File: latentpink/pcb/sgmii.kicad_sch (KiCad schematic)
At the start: 6 parts, among them J3 RJ45, J4 RJ45, U5 DP83867, U6 DP83867, U7 BEL_FUSE_S558-5999-M8-F, U8 BEL_FUSE_S558-5999-M8-F

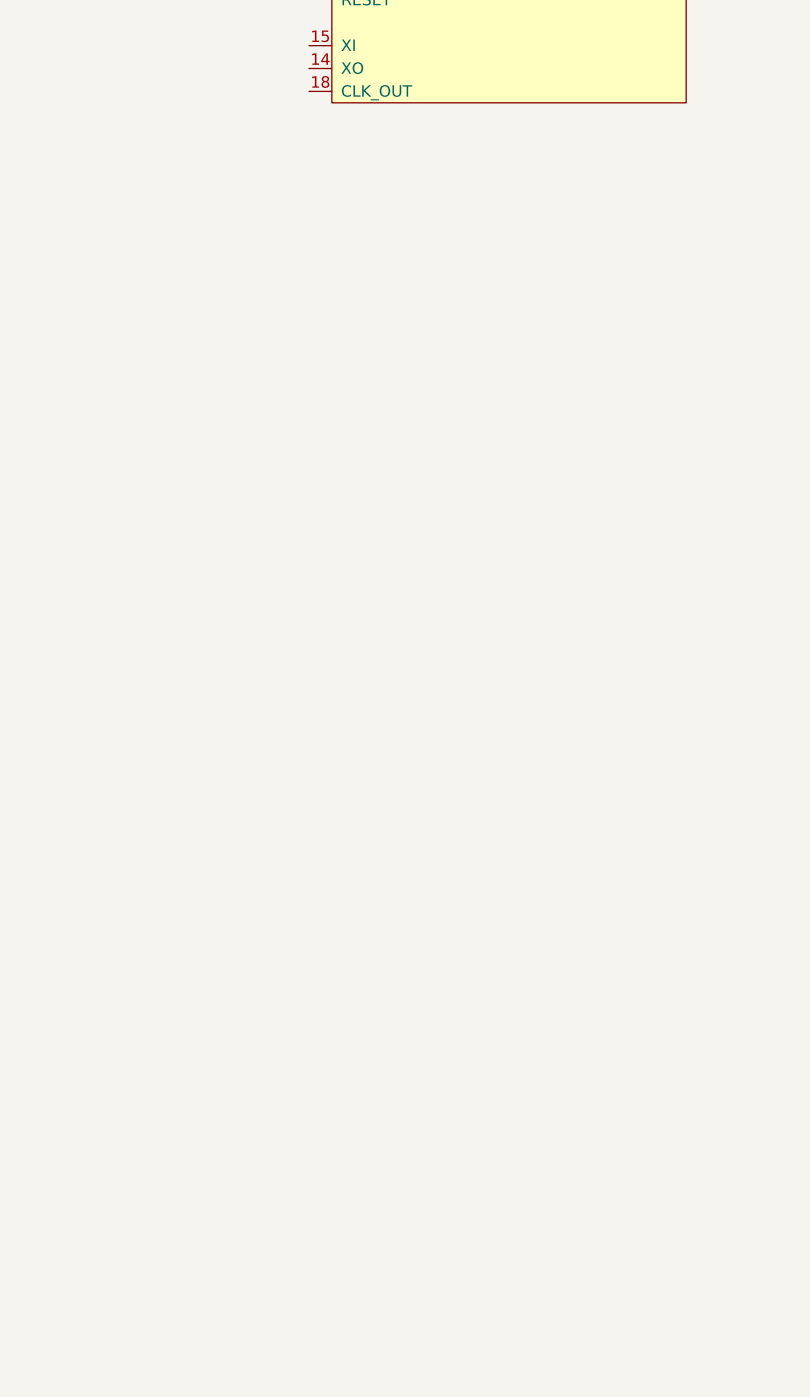
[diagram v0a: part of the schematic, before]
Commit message: Continued initial schematic capture
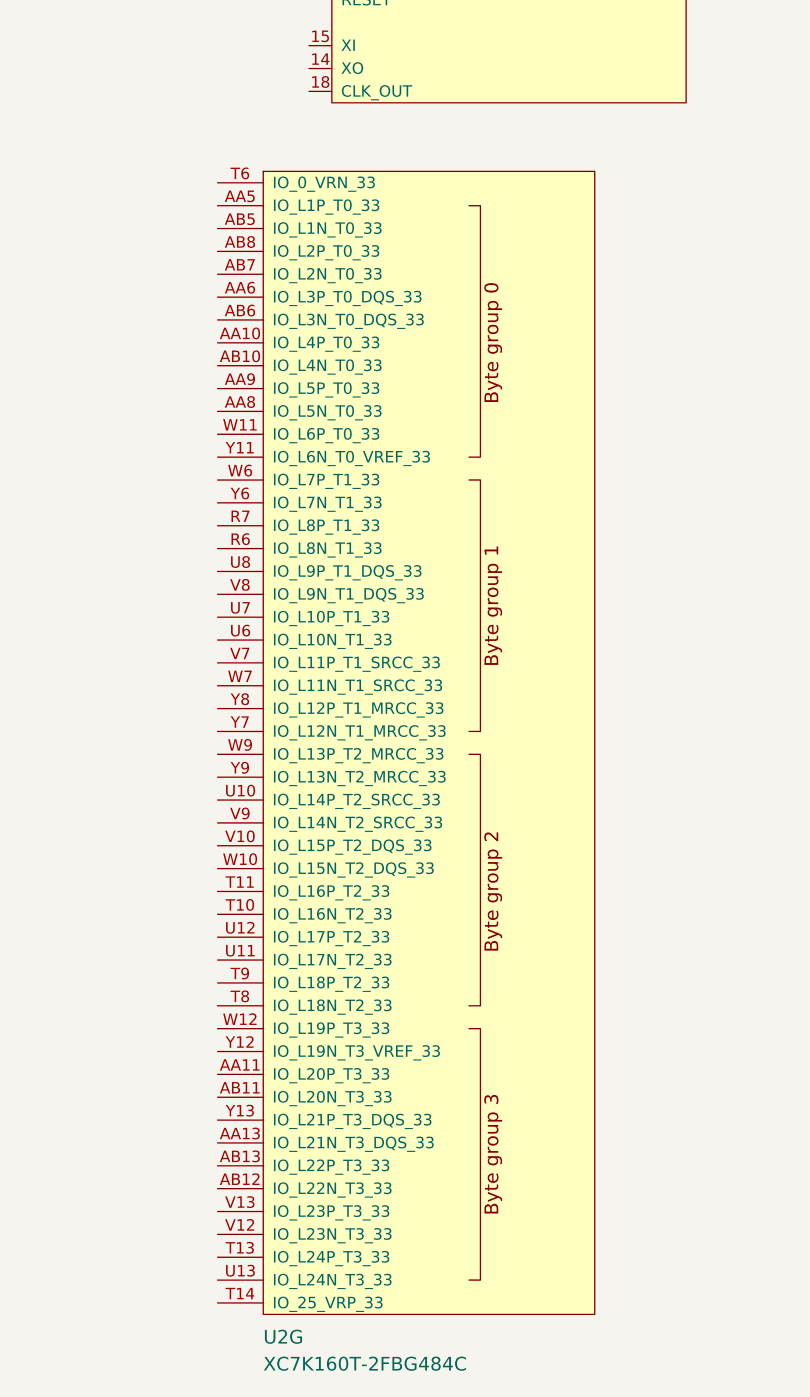
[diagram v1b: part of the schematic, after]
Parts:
- added U2: XC7K160T-2FBG484C, azonenberg_pcb:BGA_484_22x22_FULLARRAY_1MM, symbol xilinx-azonenberg:XC7KxT-FBG484

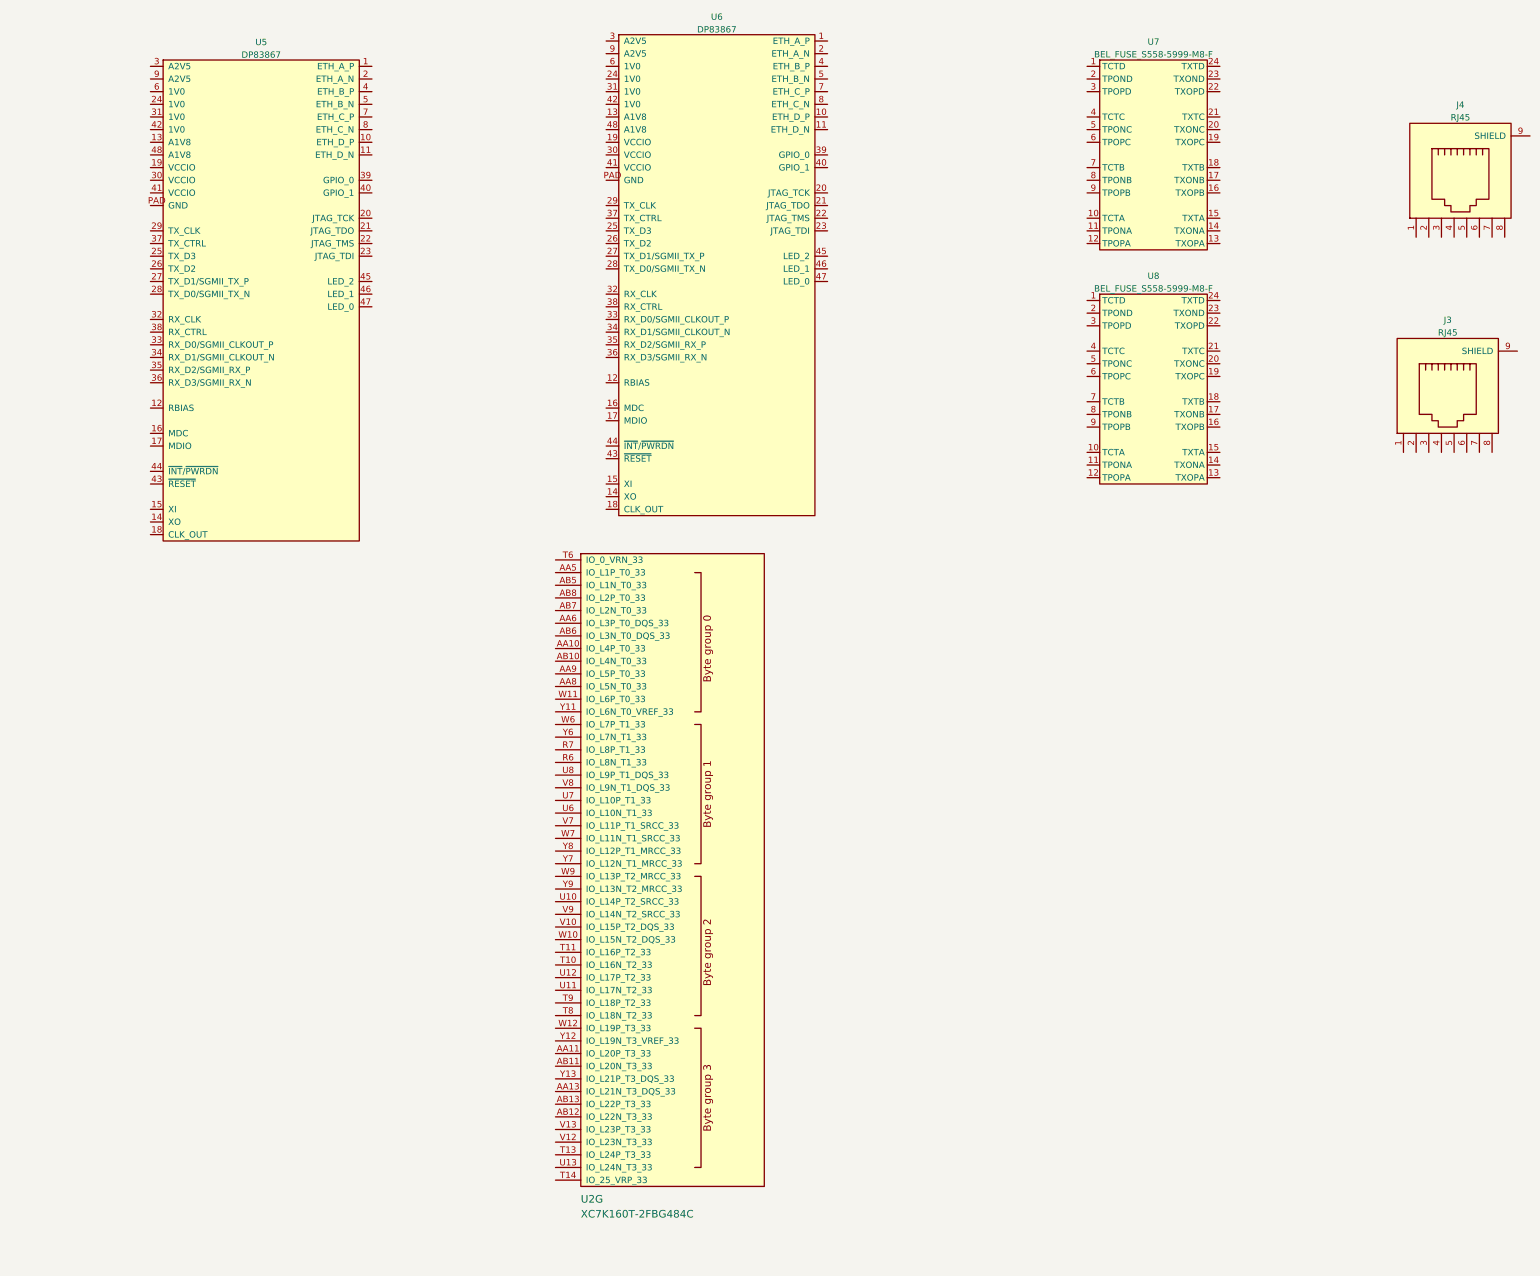
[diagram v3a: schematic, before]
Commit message: Switched to new RJ45 for LATENTPINK, continued general PHY schematic
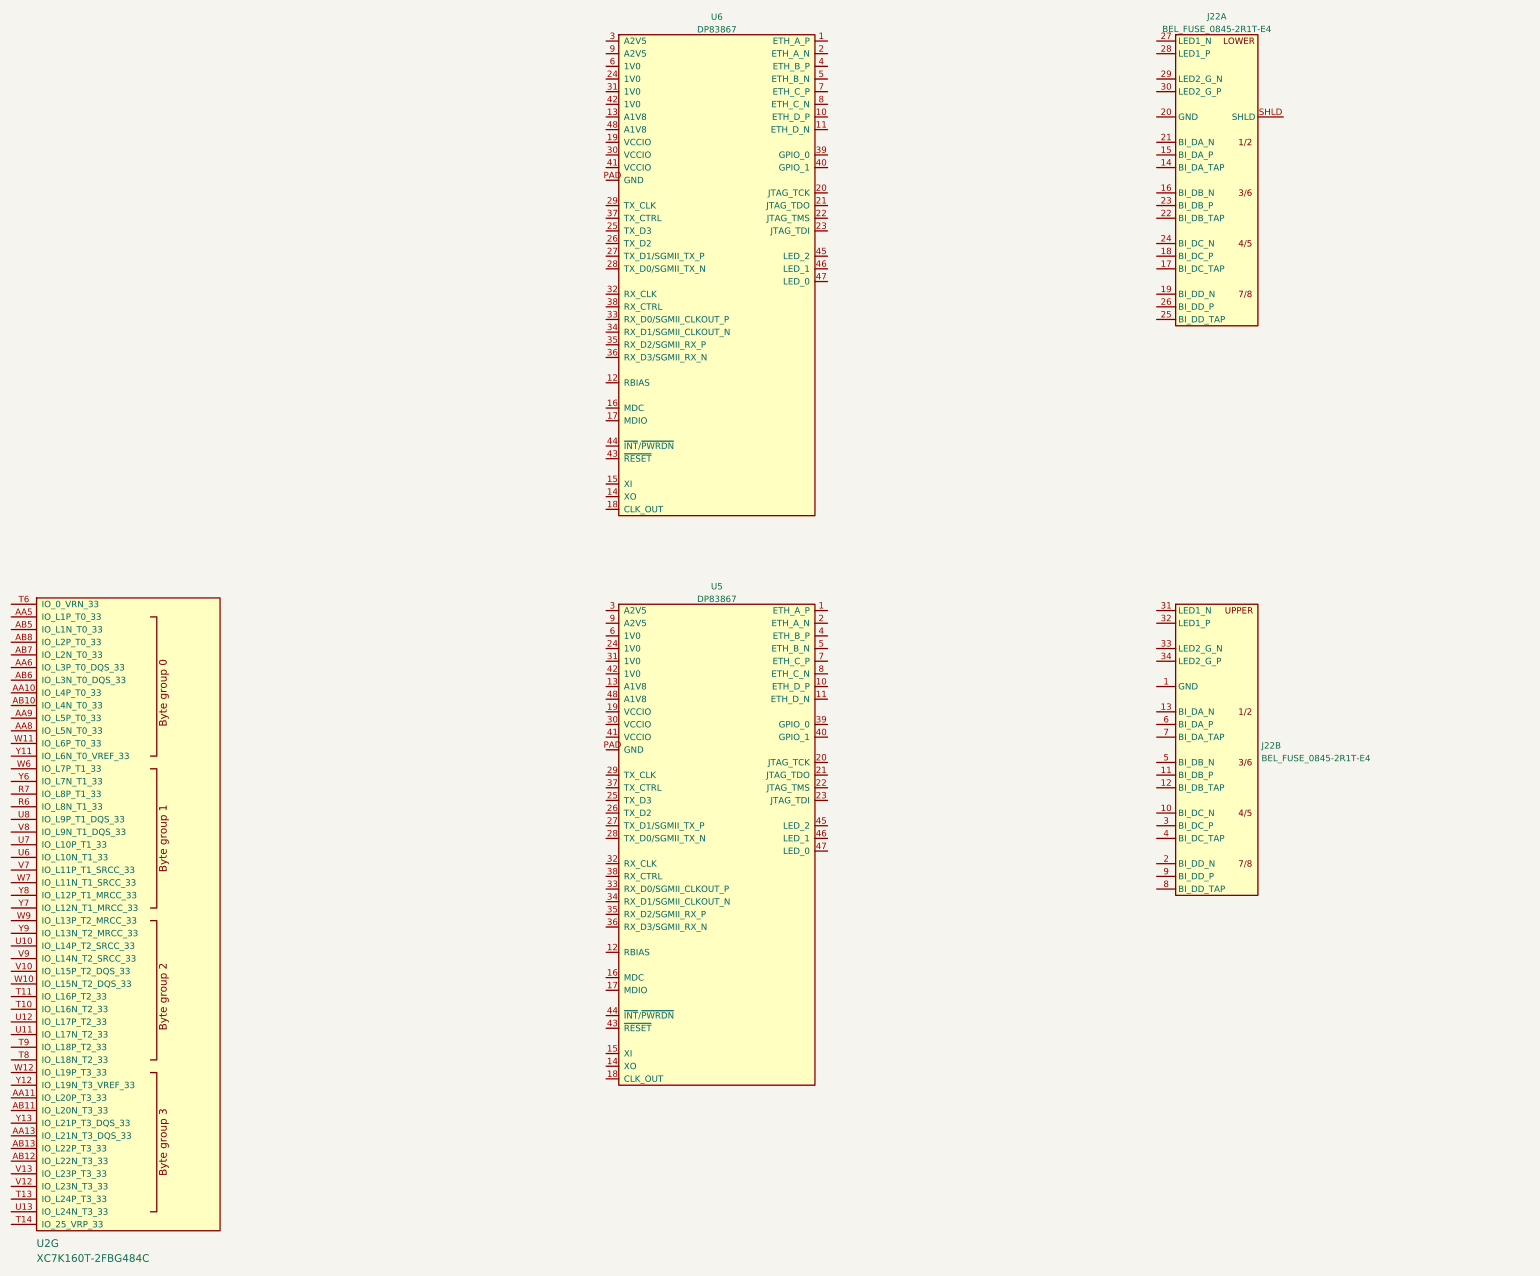
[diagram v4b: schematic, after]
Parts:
- removed J3, J4: RJ45, azonenberg_pcb:CONN_RJ45_BELSTEWART_SS-7188S-A-PG4-1-BA-xx, symbol conn:RJ45
- removed U7, U8: BEL_FUSE_S558-5999-M8-F, azonenberg_pcb:BELFUSE_S558-5999-M8-F, symbol special-azonenberg:BEL_FUSE_S558-5999-M8-F
- added J22: BEL_FUSE_0845-2R1T-E4, azonenberg_pcb:CONN_RJ45_BELFUSE_0845-2R1T-E4, symbol special-azonenberg:BEL_FUSE_0845-2R1T-E4
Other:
- moved on the sheet: U2G, U5
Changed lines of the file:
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@@
   (paper "A3")
   (title_block
-    (date "2023-05-14")
+    (date "2023-05-15")
     (rev "0.1")
     (company "Antikernel Labs")
     (comment 1 "Andrew D. Zonenberg")
   )
-  (symbol (lib_id "conn:RJ45") (at 330.2 54.61 0) (unit 1)
+  (symbol (lib_id "special-azonenberg:BEL_FUSE_0845-2R1T-E4") (at 273.05 198.12 0) (unit 2)
     (in_bom yes) (on_board yes) (fields_autoplaced)
-    (property "Reference" "J4" (id 0) (at 330.2 39.4802 0))
-    (property "Value" "RJ45" (id 1) (at 330.2 42.0171 0))
-    (property "Footprint" "azonenberg_pcb:CONN_RJ45_BELSTEWART_SS-7188S-A-PG4-1-BA-xx" (id 2) (at 330.2 54.61 0)
+    (property "Reference" "J22" (id 0) (at 290.2712 168.0753 0)
+      (effects (font (size 1.27 1.27)) (justify left))
+    )
+    (property "Value" "BEL_FUSE_0845-2R1T-E4" (id 1) (at 290.2712 170.6122 0)
+      (effects (font (size 1.27 1.27)) (justify left))
+    )
+    (property "Footprint" "azonenberg_pcb:CONN_RJ45_BELFUSE_0845-2R1T-E4" (id 2) (at 273.05 198.12 0)
       (effects (font (size 1.27 1.27)) hide)
     )
-    (property "Datasheet" "" (id 3) (at 330.2 54.61 0)
+    (property "Datasheet" "" (id 3) (at 273.05 198.12 0)
       (effects (font (size 1.27 1.27)) hide)
     )
+    (pin "14")
+    (pin "15")
+    (pin "16")
+    (pin "17")
+    (pin "18")
+    (pin "19")
+    (pin "20")
+    (pin "21")
+    (pin "22")
+    (pin "23")
+    (pin "24")
+    (pin "25")
+    (pin "26")
+    (pin "27")
+    (pin "28")
+    (pin "29")
+    (pin "30")
+    (pin "SHLD")
     (pin "1")
+    (pin "10")
+    (pin "11")
+    (pin "12")
+    (pin "13")
     (pin "2")
     (pin "3")
+    (pin "31")
+    (pin "32")
+    (pin "33")
+    (pin "34")
     (pin "4")
     (pin "5")
@@
     (pin "PAD")
   )
-  (symbol (lib_id "special-azonenberg:BEL_FUSE_S558-5999-M8-F") (at 257.81 68.58 0) (unit 1)
+  (symbol (lib_id "special-azonenberg:DP83867") (at 161.29 236.22 0) (unit 1)
     (in_bom yes) (on_board yes) (fields_autoplaced)
-    (property "Reference" "U7" (id 0) (at 268.605 26.831 0))
-    (property "Value" "BEL_FUSE_S558-5999-M8-F" (id 1) (at 268.605 29.3679 0))
-    (property "Footprint" "azonenberg_pcb:BELFUSE_S558-5999-M8-F" (id 2) (at 257.81 68.58 0)
+    (property "Reference" "U5" (id 0) (at 180.975 136.1272 0))
+    (property "Value" "DP83867" (id 1) (at 180.975 138.6641 0))
+    (property "Footprint" "azonenberg_pcb:QFN_48_0.5MM_7x7MM" (id 2) (at 163.83 237.49 0)
       (effects (font (size 1.27 1.27)) hide)
     )
-    (property "Datasheet" "" (id 3) (at 257.81 68.58 0)
-      (effects (font (size 1.27 1.27)) hide)
-    )
-    (pin "1")
-    (pin "10")
-    (pin "11")
-    (pin "12")
-    (pin "13")
-    (pin "14")
-    (pin "15")
-    (pin "16")
-    (pin "17")
-    (pin "18")
-    (pin "19")
-    (pin "2")
-    (pin "20")
-    (pin "21")
-    (pin "22")
-    (pin "23")
-    (pin "24")
-    (pin "3")
-    (pin "4")
-    (pin "5")
-    (pin "6")
-    (pin "7")
-    (pin "8")
-    (pin "9")
-  )
-  (symbol (lib_id "special-azonenberg:BEL_FUSE_S558-5999-M8-F") (at 257.81 115.57 0) (unit 1)
-    (in_bom yes) (on_board yes) (fields_autoplaced)
-    (property "Reference" "U8" (id 0) (at 268.605 73.821 0))
-    (property "Value" "BEL_FUSE_S558-5999-M8-F" (id 1) (at 268.605 76.3579 0))
-    (property "Footprint" "azonenberg_pcb:BELFUSE_S558-5999-M8-F" (id 2) (at 257.81 115.57 0)
-      (effects (font (size 1.27 1.27)) hide)
-    )
-    (property "Datasheet" "" (id 3) (at 257.81 115.57 0)
-      (effects (font (size 1.27 1.27)) hide)
-    )
-    (pin "1")
-    (pin "10")
-    (pin "11")
-    (pin "12")
-    (pin "13")
-    (pin "14")
-    (pin "15")
-    (pin "16")
-    (pin "17")
-    (pin "18")
-    (pin "19")
-    (pin "2")
-    (pin "20")
-    (pin "21")
-    (pin "22")
-    (pin "23")
-    (pin "24")
-    (pin "3")
-    (pin "4")
-    (pin "5")
-    (pin "6")
-    (pin "7")
-    (pin "8")
-    (pin "9")
-  )
-  (symbol (lib_id "special-azonenberg:DP83867") (at 69.85 127 0) (unit 1)
-    (in_bom yes) (on_board yes) (fields_autoplaced)
-    (property "Reference" "U5" (id 0) (at 89.535 26.9072 0))
-    (property "Value" "DP83867" (id 1) (at 89.535 29.4441 0))
-    (property "Footprint" "azonenberg_pcb:QFN_48_0.5MM_7x7MM" (id 2) (at 72.39 128.27 0)
-      (effects (font (size 1.27 1.27)) hide)
-    )
-    (property "Datasheet" "" (id 3) (at 72.39 128.27 0)
+    (property "Datasheet" "" (id 3) (at 163.83 237.49 0)
       (effects (font (size 1.27 1.27)) hide)
     )
@@
     (pin "PAD")
   )
-  (symbol (lib_id "conn:RJ45") (at 327.66 97.79 0) (unit 1)
-    (in_bom yes) (on_board yes) (fields_autoplaced)
-    (property "Reference" "J3" (id 0) (at 327.66 82.6602 0))
-    (property "Value" "RJ45" (id 1) (at 327.66 85.1971 0))
-    (property "Footprint" "azonenberg_pcb:CONN_RJ45_BELSTEWART_SS-7188S-A-PG4-1-BA-xx" (id 2) (at 327.66 97.79 0)
-      (effects (font (size 1.27 1.27)) hide)
-    )
-    (property "Datasheet" "" (id 3) (at 327.66 97.79 0)
-      (effects (font (size 1.27 1.27)) hide)
-    )
-    (pin "1")
-    (pin "2")
-    (pin "3")
-    (pin "4")
-    (pin "5")
-    (pin "6")
-    (pin "7")
-    (pin "8")
-    (pin "9")
-  )
-  (symbol (lib_id "xilinx-azonenberg:XC7KxT-FBG484") (at 153.67 255.27 0) (unit 7)
+  (symbol (lib_id "xilinx-azonenberg:XC7KxT-FBG484") (at 44.45 264.16 0) (unit 7)
     (in_bom yes) (on_board yes)
-    (property "Reference" "U2" (id 0) (at 153.67 259.08 0)
+    (property "Reference" "U2" (id 0) (at 44.45 267.97 0)
       (effects (font (size 1.524 1.524)) (justify left))
     )
-    (property "Value" "XC7K160T-2FBG484C" (id 1) (at 153.67 262.0734 0)
+    (property "Value" "XC7K160T-2FBG484C" (id 1) (at 44.45 270.9634 0)
       (effects (font (size 1.524 1.524)) (justify left))
     )
-    (property "Footprint" "azonenberg_pcb:BGA_484_22x22_FULLARRAY_1MM" (id 2) (at 153.67 262.89 0)
+    (property "Footprint" "azonenberg_pcb:BGA_484_22x22_FULLARRAY_1MM" (id 2) (at 44.45 271.78 0)
       (effects (font (size 1.524 1.524)) hide)
     )
-    (property "Datasheet" "" (id 3) (at 153.67 262.89 0)
+    (property "Datasheet" "" (id 3) (at 44.45 271.78 0)
       (effects (font (size 1.524 1.524)))
     )
@@
     (pin "Y5")
   )
+  (symbol (lib_id "special-azonenberg:BEL_FUSE_0845-2R1T-E4") (at 273.05 83.82 0) (unit 1)
+    (in_bom yes) (on_board yes) (fields_autoplaced)
+    (property "Reference" "J22" (id 0) (at 281.305 21.751 0))
+    (property "Value" "BEL_FUSE_0845-2R1T-E4" (id 1) (at 281.305 24.2879 0))
+    (property "Footprint" "azonenberg_pcb:CONN_RJ45_BELFUSE_0845-2R1T-E4" (id 2) (at 273.05 83.82 0)
+      (effects (font (size 1.27 1.27)) hide)
+    )
+    (property "Datasheet" "" (id 3) (at 273.05 83.82 0)
+      (effects (font (size 1.27 1.27)) hide)
+    )
+    (pin "14")
+    (pin "15")
+    (pin "16")
+    (pin "17")
+    (pin "18")
+    (pin "19")
+    (pin "20")
+    (pin "21")
+    (pin "22")
+    (pin "23")
+    (pin "24")
+    (pin "25")
+    (pin "26")
+    (pin "27")
+    (pin "28")
+    (pin "29")
+    (pin "30")
+    (pin "SHLD")
+    (pin "1")
+    (pin "10")
+    (pin "11")
+    (pin "12")
+    (pin "13")
+    (pin "2")
+    (pin "3")
+    (pin "31")
+    (pin "32")
+    (pin "33")
+    (pin "34")
+    (pin "4")
+    (pin "5")
+    (pin "6")
+    (pin "7")
+    (pin "8")
+    (pin "9")
+  )
 )
